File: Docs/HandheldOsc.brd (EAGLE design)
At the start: 100 x 80 mm, 16 parts, among them J1 BNC5-J-P-GN-RA-BH2D, U1 LMH6503MAX/NOPB, X1 SSW-106-02-G-D-RA, X2 SSW-105-02-G-D-RA

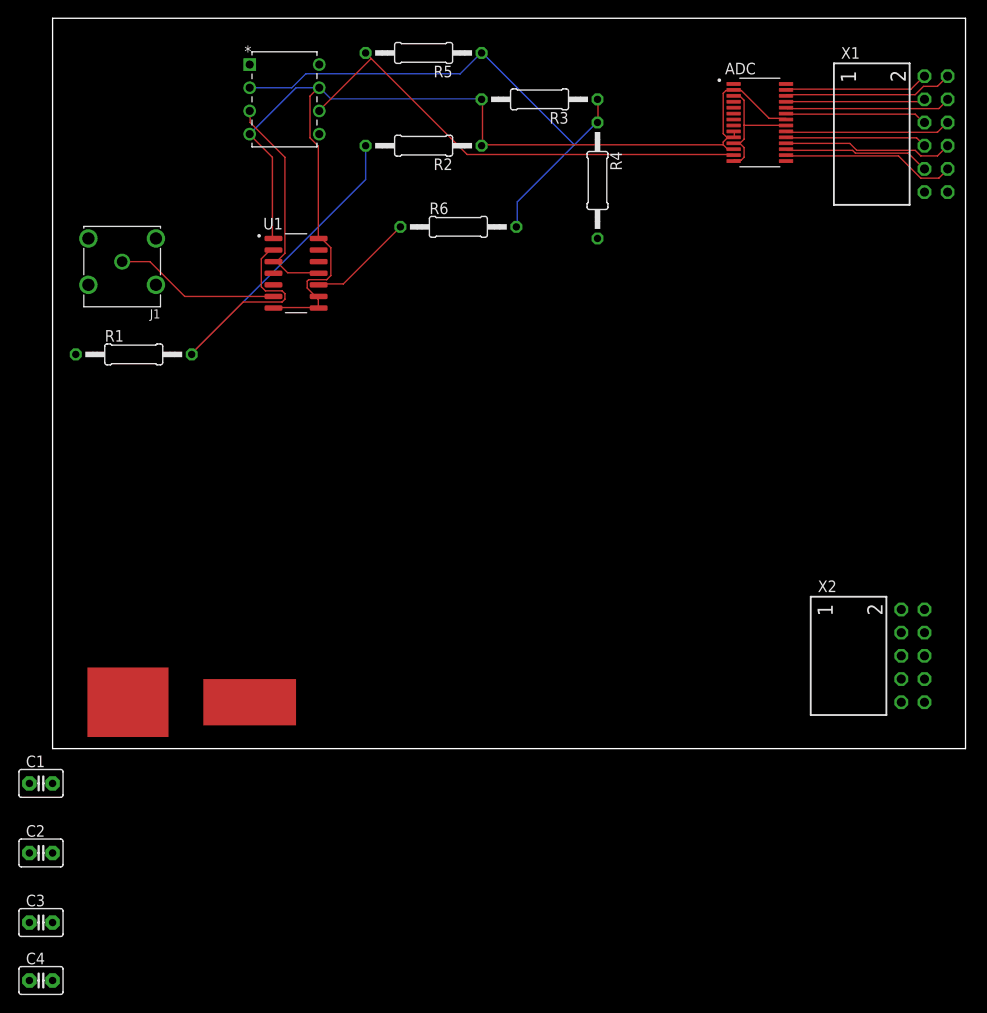
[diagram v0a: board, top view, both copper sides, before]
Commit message: DAB Board V1.1
DAB Board V1.1 (order on JLCPCB)
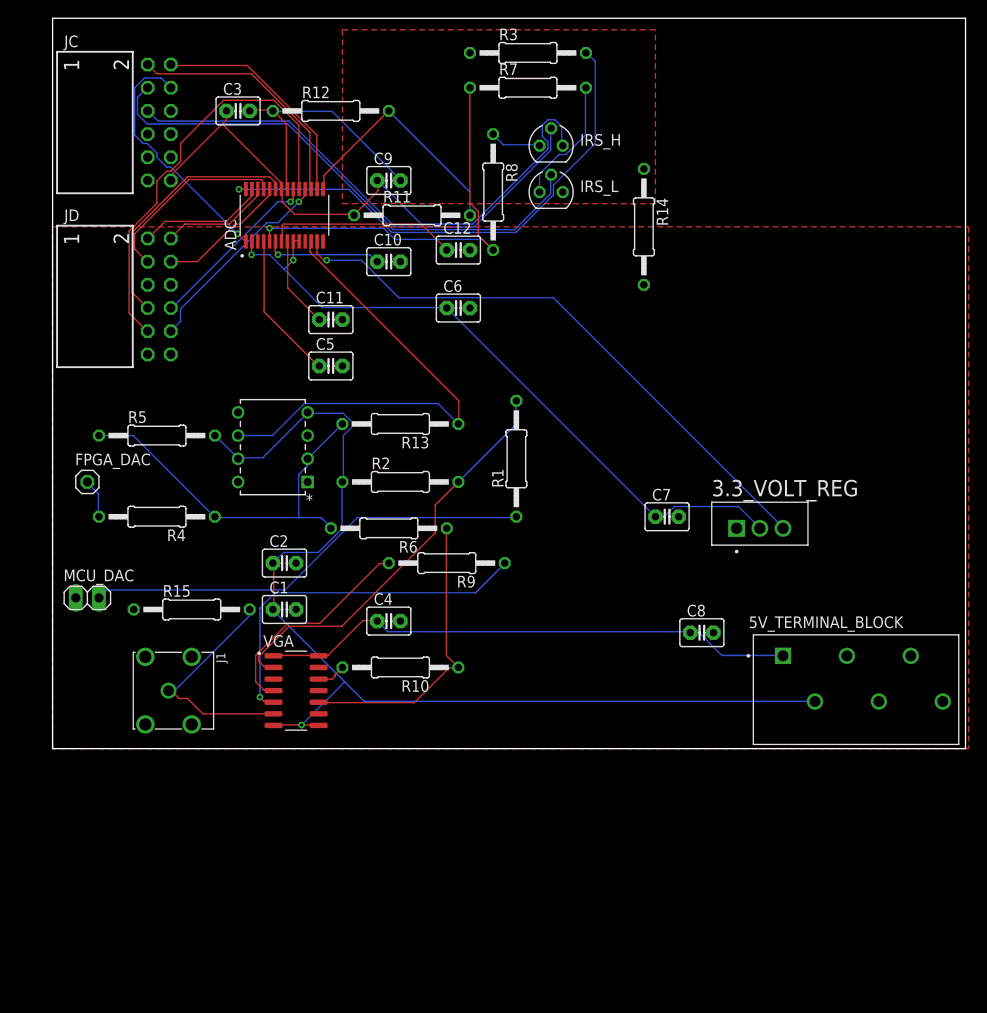
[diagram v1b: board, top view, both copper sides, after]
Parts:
- removed U1: LMH6503MAX/NOPB, LMH6503MAX_NOPB:SOIC127P600X175-14N
- removed X1: SSW-106-02-G-D-RA, con-samtec:SSW-106-02-G-D-RA
- removed X2: SSW-105-02-G-D-RA, con-samtec:SSW-105-02-G-D-RA
- added 3.3_VOLT_REG: LMS1587CT-3.3, LMS1587CT-3.3:TO254P1054X470X1955-3
- added 5V_TERMINAL_BLOCK: TBL002A-350-06GY-2GY, TBL002A-350-06GY-2GY:CUI_TBL002A-350-06GY-2GY
- added C10, C11, C12, C5, C6, C7, C8, C9: (no value), capacitor-wima:C2.5-3
- added FPGA_DAC: (no value), pinhead:1X01
- added IRS_H: BS250, transistor-small-signal:SOT54E
- added IRS_L: BS170, transistor-small-signal:SOT54E
- added JC, JD: SSW-106-02-G-D-RA, con-samtec:SSW-106-02-G-D-RA
- added MCU_DAC: (no value), pinhead:1X02
- added R10, R11, R12, R13, R14, R15, R7, R8, R9: (no value), rcl:0207/12
- added VGA: LMH6503MAX/NOPB, LMH6503MAX_NOPB:SOIC127P600X175-14N
- C1, C2: value 1 uF -> (none)
- C3, C4: value 1uF -> (none)
- moved C3 91.5 mm to (20.3, 69.8)
- moved R4 60.7 mm to (11.4, 25.4), turned to 180 degrees
- moved C4 54.8 mm to (36.8, 14.0)
- moved ADC 53.1 mm to (25.4, 58.4), turned to 90 degrees
- moved R5 51.1 mm to (11.4, 34.3), turned to 0 degrees
- moved J1 47.3 mm to (12.7, 6.35), turned to 270 degrees
- moved R1 43.4 mm to (50.8, 31.8), turned to 90 degrees
- moved C2 41.5 mm to (25.4, 20.3)
- moved R2 36.9 mm to (38.1, 29.2), turned to 0 degrees
- moved R6 33.9 mm to (36.8, 24.1), turned to 180 degrees
- moved C1 32.8 mm to (25.4, 15.2)
- moved AMPLIFIER 31.8 mm to (20.3, 36.8), turned to 180 degrees
- moved R3 5.24 mm to (52.1, 76.2), turned to 0 degrees
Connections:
- removed net 0: AMPLIFIER.3, U1.11, U1.3
- removed net N$10: ADC.25, X1.3
- removed net N$11: ADC.24, X1.4
- removed net N$12: ADC.23, X1.5
- removed net N$13: ADC.20, X1.6
- removed net N$14: ADC.19, X1.7
- removed net N$15: ADC.18, X1.8
- removed net N$16: ADC.17, X1.9
- removed net N$17: ADC.16, X1.10
- removed net N$18: ADC.6, C1.2, C2.2
- removed net N$19: X1.12
- removed net N$20: ADC.28
- removed net N$21: ADC.11, ADC.14, ADC.3, C1.1
- removed net N$22: ADC.1
- removed net N$23: ADC.22, C4.1
- removed net N$24: C3.2, C4.2
- removed net N$25: ADC.21, C3.1
- removed net N$3: ADC.13, AMPLIFIER.6, R5.2
- removed net N$4: R4.2
- removed net N$5: R1.1
- removed net N$6: J1.1, U1.6
- removed net N$7: ADC.27, X1.1
- removed net N$8: R1.2, R2.2, U1.2
- removed net N$9: ADC.26, X1.2
- new net +3V3: 3.3_VOLT_REG.2, ADC.10, ADC.2, ADC.9, C6.1, C7.1
- new net +5V: 5V_TERMINAL_BLOCK.1, C4.1, C8.1, VGA.1, VGA.14
- new net -5V: 5V_TERMINAL_BLOCK.2, AMPLIFIER.4, AMPLIFIER.7, C1.1, C2.1, R2.1, R5.2, VGA.7, VGA.8
- new net ADC_DF: ADC.15, R11.2, R12.2
- new net ADC_IRS: ADC.5, R7.1, R8.2
- new net ADC_STDBY: ADC.28, R3.2
- new net ADC_VCOM: ADC.4, C5.1
- new net ADC_VIN+: 3.3_VOLT_REG.3, ADC.13
- new net ADC_VIN-: ADC.12, AMPLIFIER.6, R13.1
- new net ADC_VREF: ADC.6, C10.1
- new net ADC_VREFB: ADC.8, C11.1
- new net ADC_VREFT: ADC.7, C12.1
- new net AGND: 3.3_VOLT_REG.1, 5V_TERMINAL_BLOCK.6, ADC.11, ADC.14, ADC.3, AMPLIFIER.3, C1.2, C10.2, C11.2, C12.2, C2.2, C4.2, C5.2, C6.2, C7.2, C8.2, J1.S_1, J1.S_2, J1.S_3, J1.S_4, MCU_DAC.1, R14.2, R15.1, VGA.11, VGA.3, VGA.9
- new net BNC: J1.1, R15.2, VGA.6
- new net DGND: ADC.21, C3.2, C9.2, IRS_L.S, R12.1, R14.1, R3.1
- new net FPGA_D0: ADC.27, JD.1
- new net FPGA_D1: ADC.26, JD.2
- new net FPGA_D2: ADC.25, JD.3
- new net FPGA_D3: ADC.24, JD.4
- new net FPGA_D4: ADC.23, JD.7
- new net FPGA_D5: ADC.20, JD.8
- new net FPGA_D6: ADC.19, JD.9
- new net FPGA_D7: ADC.18, JD.10
- new net FPGA_D8: ADC.17, JC.1
- new net FPGA_D9: ADC.16, JC.2
- new net FPGA_SAMPLE_CLK: ADC.1, JC.4
- new net FPGA_VOFFSET: FPGA_DAC.1, R4.2
- new net GAIN_CONTROL: MCU_DAC.2, R1.1
- new net JC1: IRS_H.G, JC.5
- new net JC7: IRS_L.G, JC.3
- new net MCU_CLK: JD.12
- new net VGA_+RG: R9.2, VGA.4
- new net VGA_-RG: R9.1, VGA.5
- new net VGA_I-: R10.2, VGA.12
- new net VGA_VG: R1.2, R2.2, VGA.2
- new net VGA_VOUT: R10.1, R6.1, VGA.10
- new net V_OFFSET: AMPLIFIER.2, R13.2, R4.1, R5.1, R6.2
- net N$1: now also IRS_H.D, R8.1; no longer R6.1, U1.10
- net N$2: now also IRS_L.D, R7.2; no longer AMPLIFIER.2, R3.1, R4.1, R5.1, R6.2
- net VCC: now also ADC.22, C3.1, C9.1, IRS_H.S, JC.12, R11.1; no longer ADC.10, ADC.12, ADC.2, ADC.9, AMPLIFIER.4, AMPLIFIER.7, C2.1, R2.1, R3.2, U1.1, U1.14, U1.7, U1.8, U1.9
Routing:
- net -5V: track 0.00 -> 120.5 mm, vias 0 -> 1
- net +3V3: track 0.00 -> 74.7 mm, vias 0 -> 2
- net ADC_VIN+: track 0.00 -> 64.9 mm, vias 0 -> 1
- net +5V: track 0.00 -> 59.1 mm
- net JC7: track 0.00 -> 57.6 mm
- net VCC: track 123.6 -> 66.6 mm
- net ADC_STDBY: track 0.00 -> 56.8 mm, vias 0 -> 1
- net JC1: track 0.00 -> 55.3 mm
- net ADC_VIN-: track 0.00 -> 53.3 mm
- net N$3: track 53.0 -> 0.00 mm
- net N$8: track 51.8 -> 0.00 mm
- net GAIN_CONTROL: track 0.00 -> 49.4 mm
- net FPGA_D6: track 0.00 -> 47.1 mm
- net ADC_IRS: track 0.00 -> 45.8 mm, vias 0 -> 1
- net VGA_VG: track 0.00 -> 45.6 mm
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- added copper zone on layer 1, net AGND
- added copper zone on layer 1, net DGND
